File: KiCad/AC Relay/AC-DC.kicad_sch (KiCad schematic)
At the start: 9 parts, among them J1 Screw_Terminal_01x02, U1 HLK-PM01, U2 BU33SD5WG-TR

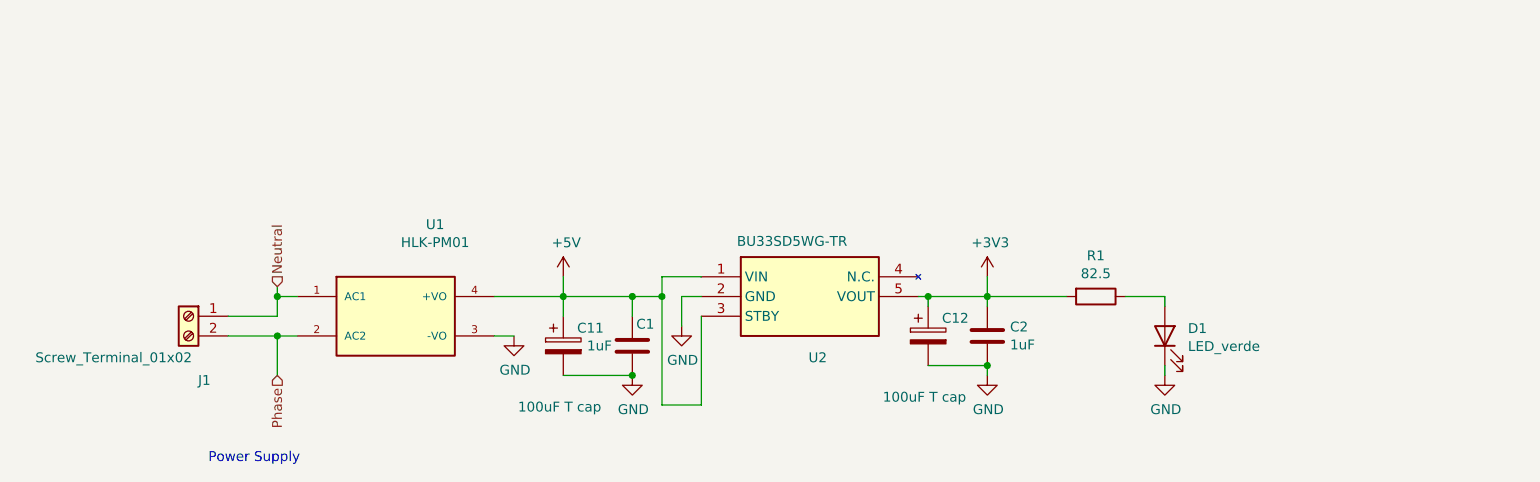
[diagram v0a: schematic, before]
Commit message: error elemination
schametic error elemination
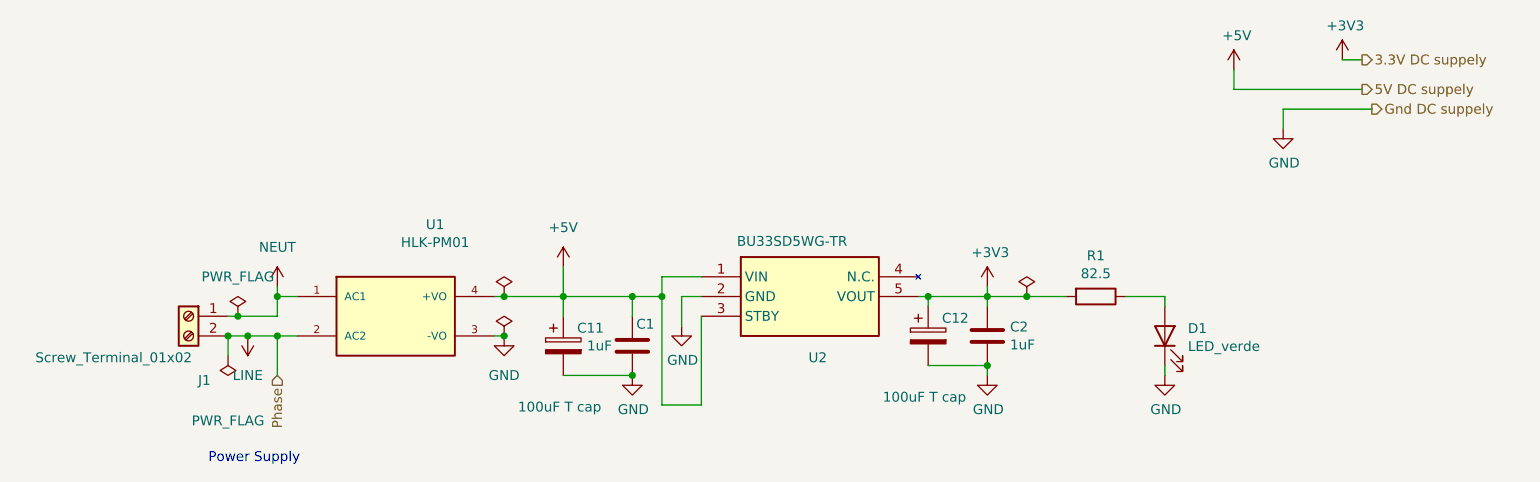
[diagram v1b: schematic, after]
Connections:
- net Neutral renamed NEUT
- net Phase renamed LINE
